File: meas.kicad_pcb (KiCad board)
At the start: 2 copper layers, 100 x 220 mm, 233 parts, among them J101 Conn_01x06_Socket, J102 Conn_01x02_Socket, J103 Conn_01x02_Socket, J104 Conn_01x02_Socket, J105 Conn_01x02_Socket, Q1001 DPLS350E, U1001 MC7805, U1101 R05C05TE05S, U1201 R05C05TE05S, U1301 R05C05TE05S, U1401 R05C05TE05S, U201 Si8641BD-B-IS2, U301 Si8641BD-B-IS2, U401 Si8641BD-B-IS2, U501 Si8641BD-B-IS2, U601 ADS8665IPWR, U701 ADS8665IPWR, U801 ADS8665IPWR, U901 ACS730xLCTR-20AB

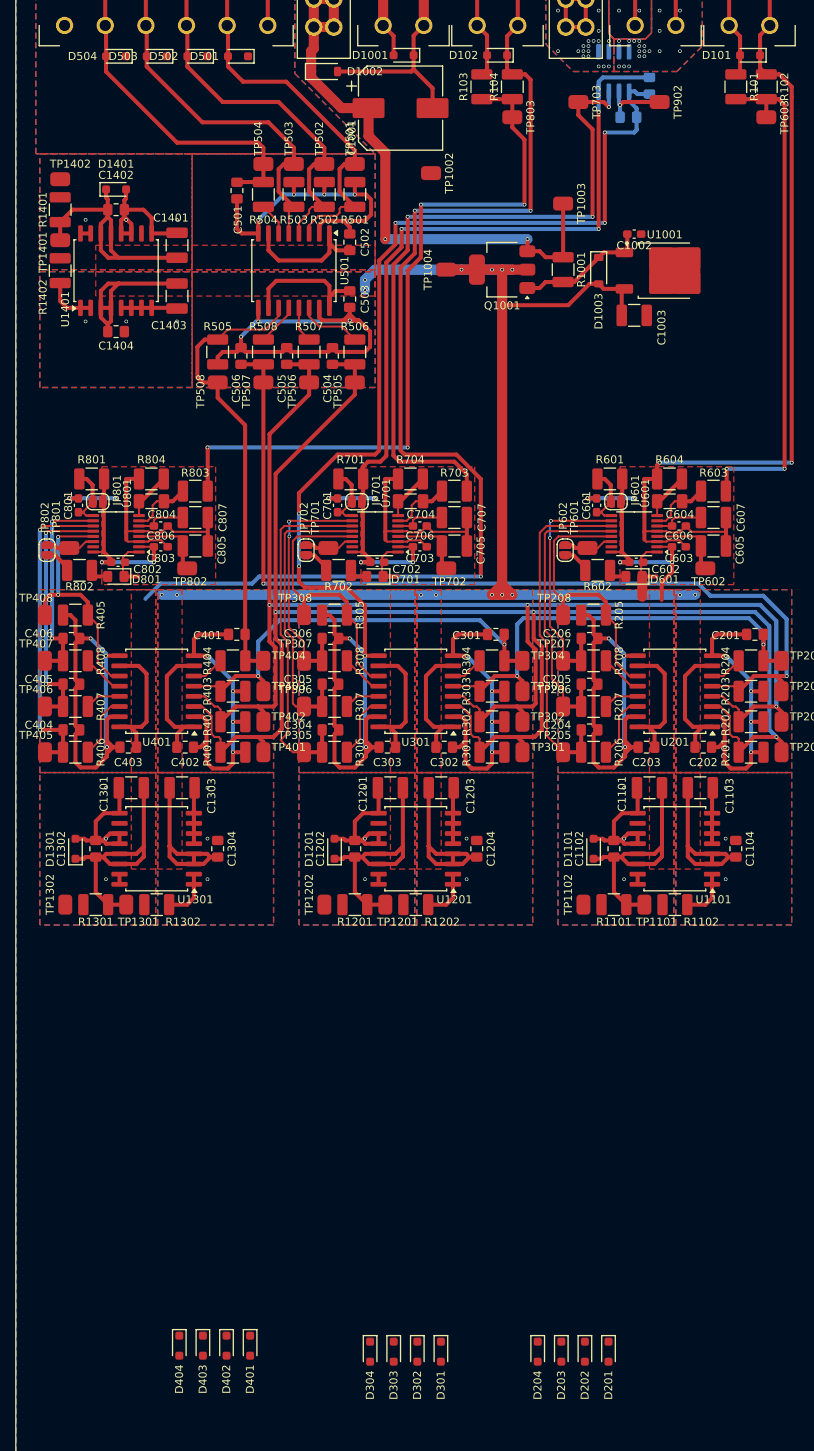
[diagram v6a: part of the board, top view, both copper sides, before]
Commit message: fix filled zone netnumbers
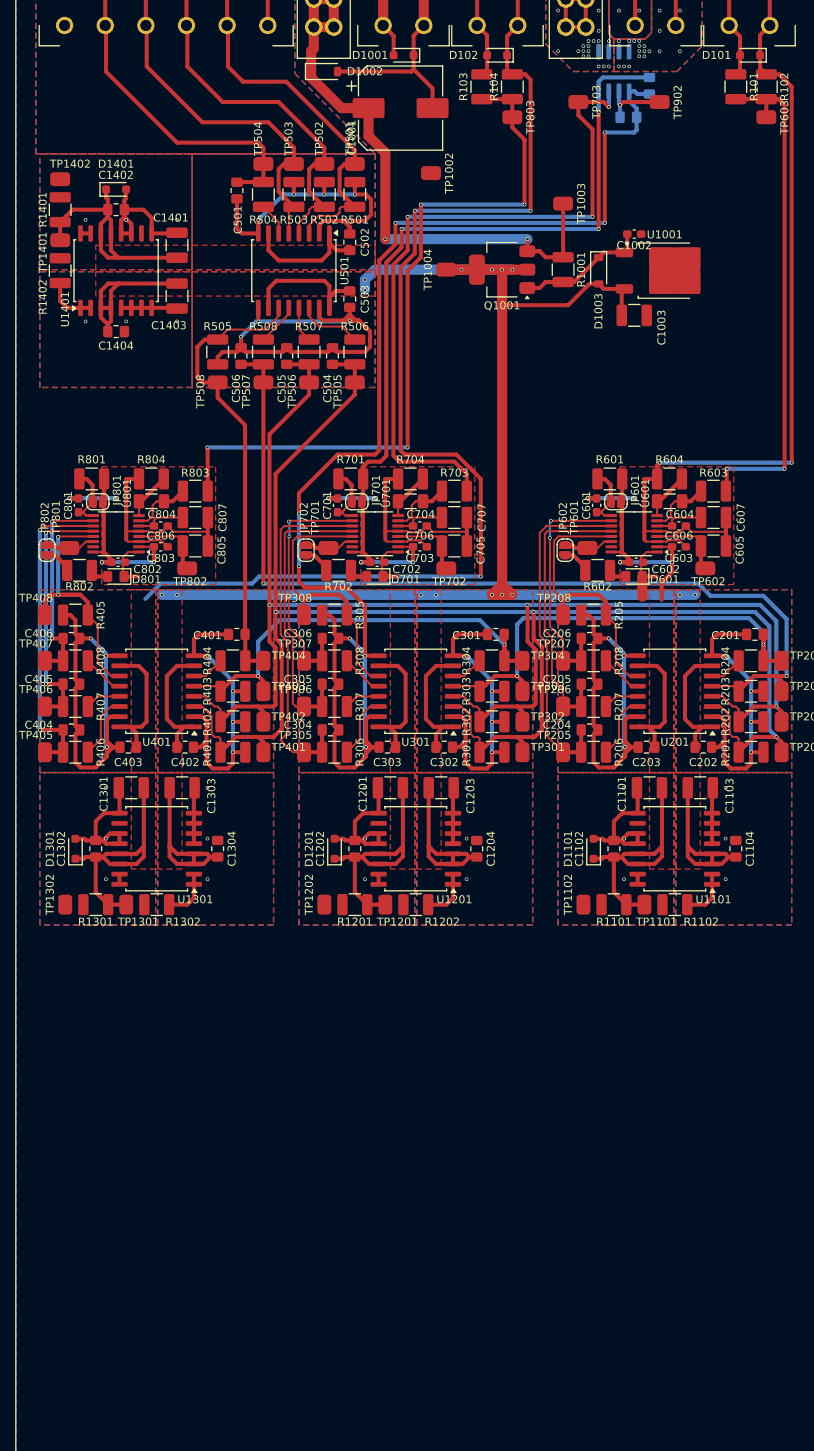
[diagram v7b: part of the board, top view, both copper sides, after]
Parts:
- removed D201, D202, D203, D204, D301, D302, D303, D304, D401, D402, D403, D404, D501, D502, D503, D504: D_TVS, meas:D_SOD-323_HandSoldering
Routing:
- net /SDIO2: track 54.3 -> 57.6 mm
- net /SDIO1: track 56.6 -> 59.9 mm
- net /adc2/SDO-0: track 31.0 -> 33.8 mm
- added copper zone on B.Cu, net /GND_ISO_I
- added copper zone on F.Cu, net /GND_ISO_I
- removed copper zone on B.Cu, net +5VA
- removed copper zone on B.Cu, net /+5VA_ISO_I
- removed copper zone on B.Cu, net /+5VA_ISO_U
- removed copper zone on B.Cu, net /adc1/SDI
- removed copper zone on F.Cu, net /adc1/SDI
- removed copper zone on F.Cu, net Net-(U701-REFCAP)

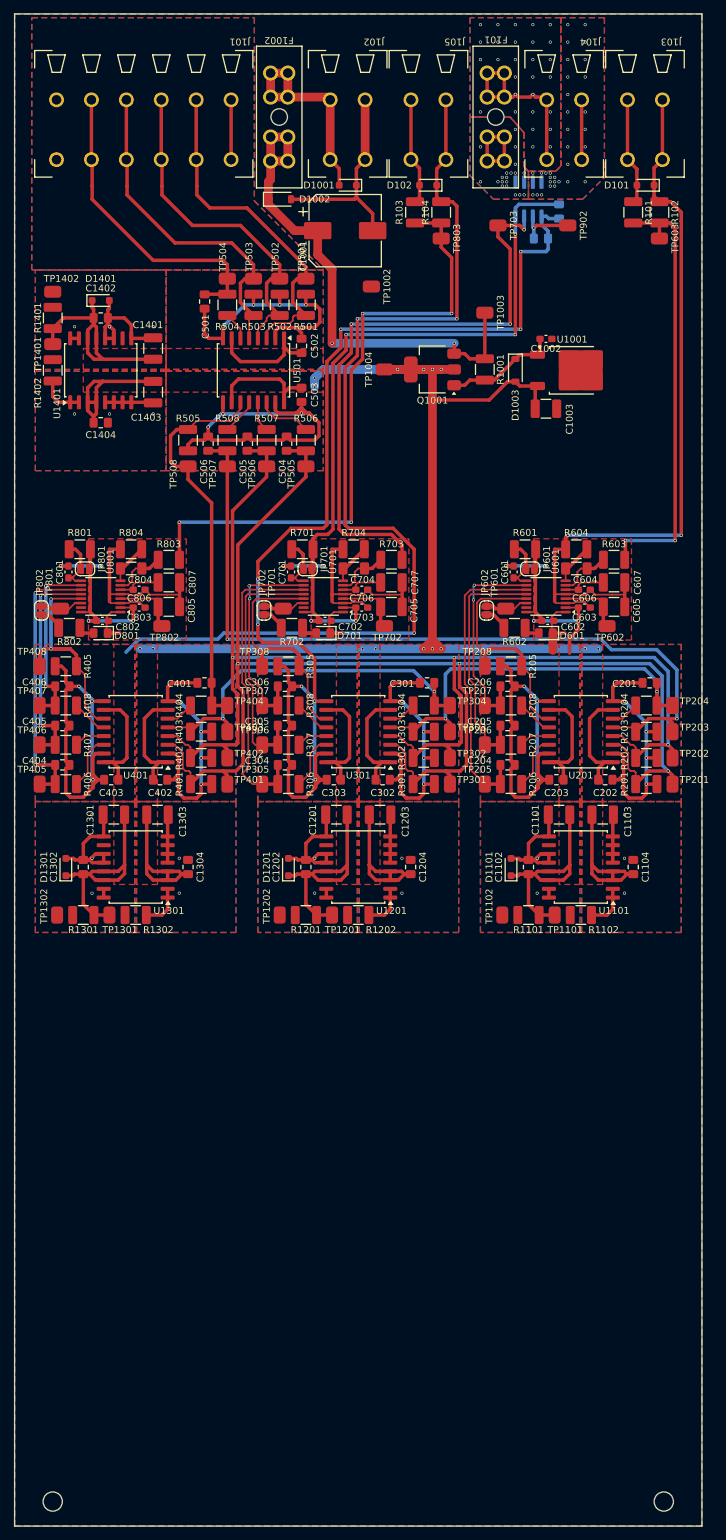
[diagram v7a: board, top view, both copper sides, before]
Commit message: resize pcb to 100x130 mm^2
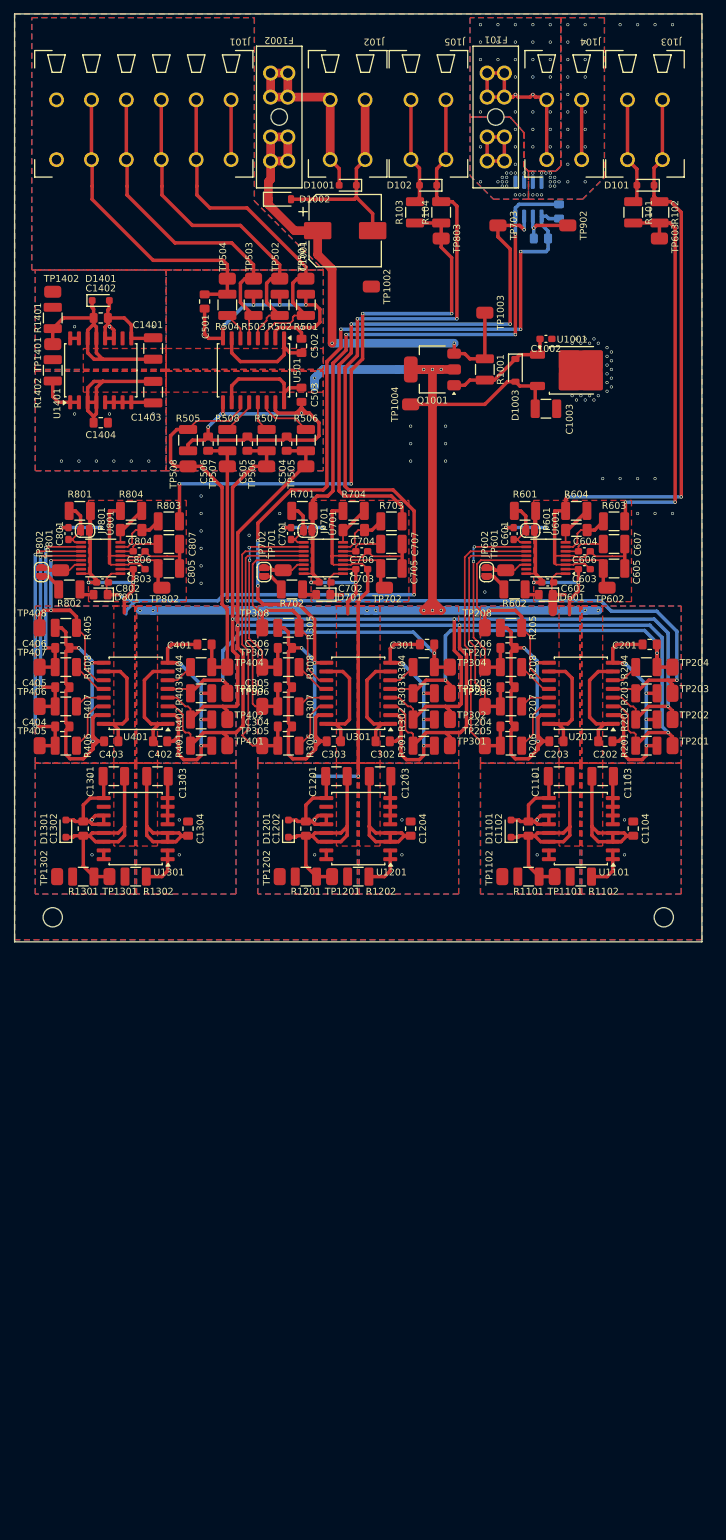
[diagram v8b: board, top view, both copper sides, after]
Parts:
- moved REF** 85.0 mm to (155.6, 171.4)
- moved REF** 85.0 mm to (244.4, 171.4)
- moved TP1004 6.35 mm to (207.6, 96.8)
- moved C1102 5.59 mm to (224.8, 158.5)
- moved C1104 5.59 mm to (240.0, 158.5)
- moved C1202 5.59 mm to (192.4, 158.5)
- moved C1204 5.59 mm to (207.6, 158.5)
- moved C1302 5.59 mm to (160.0, 158.5)
- moved C1304 5.59 mm to (175.2, 158.5)
- moved C201 5.59 mm to (242.4, 131.7)
- moved C301 5.59 mm to (210.0, 131.7)
- moved C401 5.59 mm to (177.6, 131.7)
- moved D1101 5.59 mm to (222.2, 158.5)
- moved D1201 5.59 mm to (189.8, 158.5)
- moved D1301 5.59 mm to (157.5, 158.5)
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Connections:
- C1301 pad 1: /adc2/GND_ADC -> /GND_ISO_T
- C1301 pad 2: /adc2/+5VA_ADC -> /+5VA_ISO_T
- C1302 pad 1: /adc2/GND_ADC -> /GND_ISO_T
- C1302 pad 2: /adc2/+5VA_ADC -> /+5VA_ISO_T
- C801 pad 1: /adc2/GND_ADC -> /GND_ISO_T
- C802 pad 1: /adc2/GND_ADC -> /GND_ISO_T
- C802 pad 2: /adc2/+5VA_ADC -> /+5VA_ISO_T
- C803 pad 1: /adc2/GND_ADC -> /GND_ISO_T
- C803 pad 2: /adc2/+5VA_ADC -> /+5VA_ISO_T
- C805 pad 1: /adc2/GND_ADC -> /GND_ISO_T
- C806 pad 1: /adc2/GND_ADC -> /GND_ISO_T
- C807 pad 1: /adc2/GND_ADC -> /GND_ISO_T
- D1301 pad 1: /adc2/+5VA_ADC -> /+5VA_ISO_T
- D1301 pad 2: /adc2/GND_ADC -> /GND_ISO_T
- D801 pad 1: /adc2/GND_ADC -> /GND_ISO_T
- JP801 pad 1: /adc2/+5VA_ADC -> /+5VA_ISO_T
- R1301 pad 1: /adc2/GND_ADC -> /GND_ISO_T
- R1301 pad 2: /adc2/+5VA_ADC -> /+5VA_ISO_T
- R1302 pad 1: /adc2/GND_ADC -> /GND_ISO_T
- R801 pad 1: /adc2/+5VA_ADC -> /+5VA_ISO_T
- R804 pad 2: /adc2/GND_ADC -> /GND_ISO_T
- TP1301 pad 1: /adc2/+5VA_ADC -> /+5VA_ISO_T
- TP1302 pad 1: /adc2/GND_ADC -> /GND_ISO_T
- U1301 pad 11: /adc2/GND_ADC -> /GND_ISO_T
- U1301 pad 12: /adc2/GND_ADC -> /GND_ISO_T
- U1301 pad 13: /adc2/+5VA_ADC -> /+5VA_ISO_T
- U1301 pad 14: /adc2/+5VA_ADC -> /+5VA_ISO_T
- U1301 pad 15: /adc2/GND_ADC -> /GND_ISO_T
- U1301 pad 16: /adc2/GND_ADC -> /GND_ISO_T
- U1301 pad 9: /adc2/GND_ADC -> /GND_ISO_T
- U801 pad 1: /adc2/GND_ADC -> /GND_ISO_T
- U801 pad 16: /adc2/+5VA_ADC -> /+5VA_ISO_T
- U801 pad 2: /adc2/+5VA_ADC -> /+5VA_ISO_T
- U801 pad 3: /adc2/GND_ADC -> /GND_ISO_T
- U801 pad 5: /adc2/GND_ADC -> /GND_ISO_T
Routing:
- net /adc2/GND_ADC: track 62.7 -> 0.00 mm, vias 5 -> 0
- net /+5VA_ISO_T: track 17.6 -> 78.8 mm, vias 0 -> 2
- net /GND_ISO_T: track 200.1 -> 260.7 mm, vias 6 -> 12
- net /adc2/+5VA_ADC: track 56.2 -> 0.00 mm, vias 2 -> 0
- net /adc1/GND_ADC: track 62.7 -> 99.8 mm, vias 5 -> 6
- net +5VA: track 322.5 -> 316.5 mm, vias 15 -> 14
- net /GND_ISO_I: track 171.5 -> 165.9 mm
- net /adc2/AIN_P: track 92.0 -> 86.4 mm
- net /adc1/AIN_P: track 87.1 -> 81.5 mm
- net /adc/AIN_P: track 64.2 -> 58.6 mm
- net /GND_ISO_U: track 204.1 -> 198.5 mm
- net /SDI: track 117.1 -> 111.5 mm
- net /~{CS}: track 198.4 -> 192.9 mm
- net /SCKL: track 179.7 -> 175.2 mm
- net /+5VA_ISO_I: track 157.6 -> 157.0 mm
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- removed copper zone on F.Cu, net /adc2/+5VA_ADC
- removed copper zone on B.Cu, net /adc2/GND_ADC
- removed copper zone on F.Cu, net /adc2/GND_ADC
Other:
- board size 100 x 220 mm -> 100 x 135 mm
